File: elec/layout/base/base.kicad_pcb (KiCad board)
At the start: 2 copper layers, 38 parts, among them U1 ?, U2 ?, U3 ?, U4 ?, U5 ?, U6 ?, U7 ?, U8 ?, U9 ?

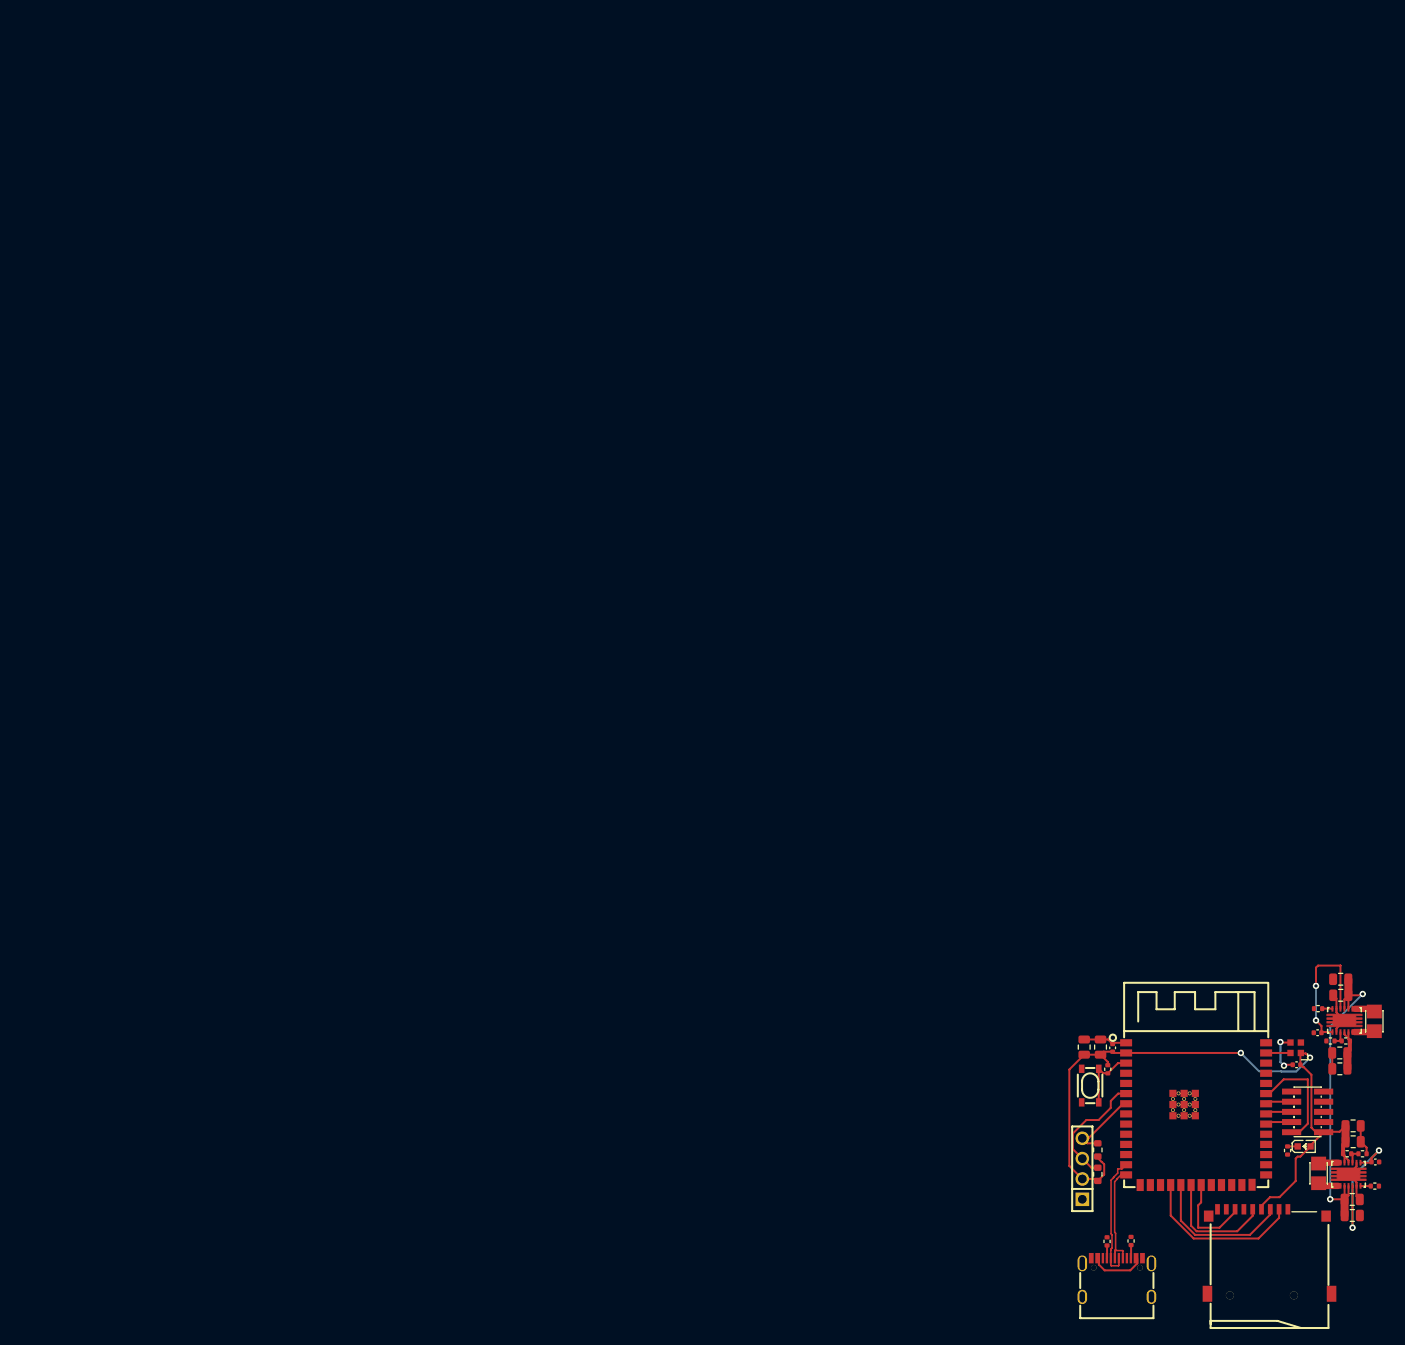
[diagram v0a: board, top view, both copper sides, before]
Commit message: run build with 0.3 compiler
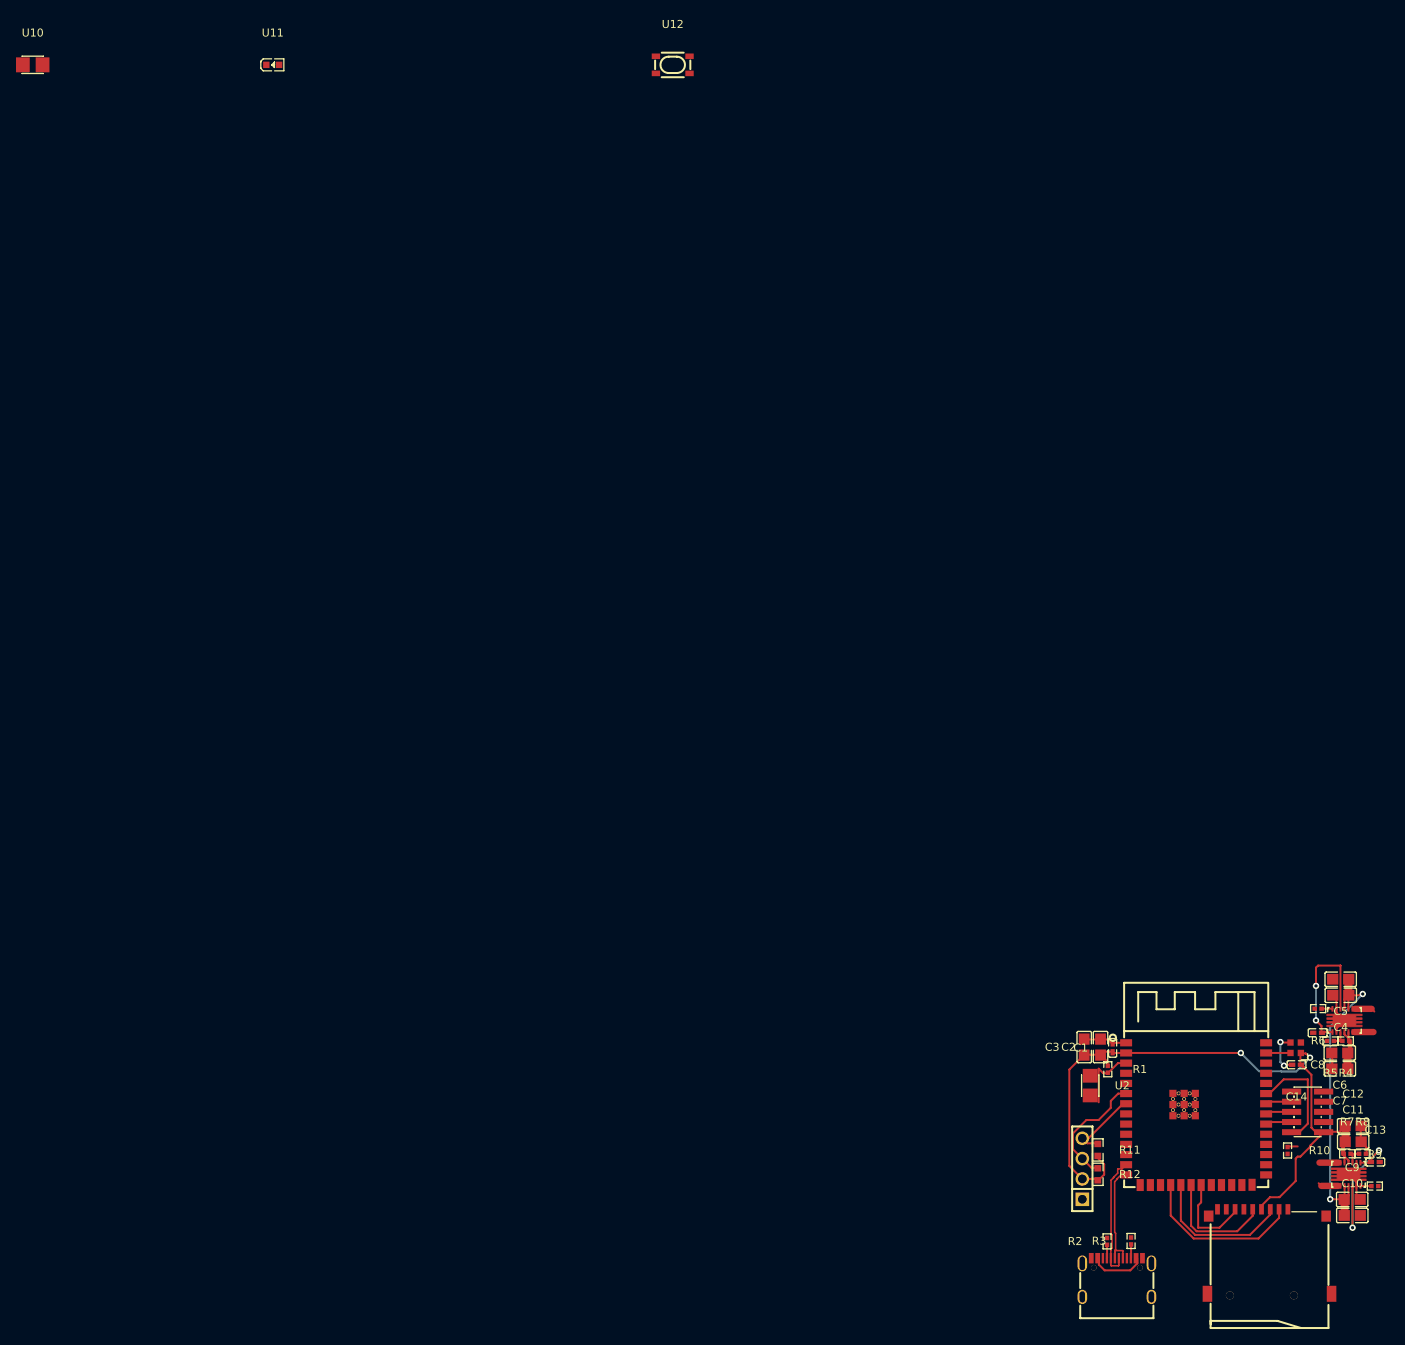
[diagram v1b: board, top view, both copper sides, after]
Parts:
- removed L1, L2: ?, lib:IND-SMD_L2.5-W2.0_WPN252012H
- removed LED1: ?, lib:LED0603-RD
- added U10: , lib:IND-SMD_L2.5-W2.0_WPN252012H, F.Cu at (50.0, 0.00)
- added U11: , lib:LED0603-RD, F.Cu at (80.0, 0.00)
- added U12: , lib:KEY-SMD_4P-L4.2-W3.2-P2.20-LS4.6, F.Cu at (130.0, 0.00)
- C1, C13, C14, C8: value 16V 100nF X7R ±10% 0402 Multilayer Ceramic Capacitors MLCC - SMD/SMT ROHS -> 100nF ±10% 16V X7R; footprint lib:C0402 -> atopile:C0402-b3ef17
- C10, C11, C12, C2, C3, C4, C5, C6, C7, C9: value 25V 10uF X5R ±10% 0805 Multilayer Ceramic Capacitors MLCC - SMD/SMT ROHS -> 10µF ±10% 25V X5R; footprint lib:C0805 -> atopile:C0805-3b2e55
- R1: value 62.5mW Thick Film Resistors 50V ±100ppm/℃ ±1% 10kΩ 0402 Chip Resistor - Surface Mount ROHS -> 10kΩ ±1% 62.5mW; footprint lib:R0402 -> atopile:R0402-56259e
- R10: value 62.5mW Thick Film Resistors 50V ±100ppm/℃ ±1% 330Ω 0402 Chip Resistor - Surface Mount ROHS -> 10kΩ ±1% 62.5mW; footprint lib:R0402 -> atopile:R0402-56259e
- R11, R12: value 100mW Thick Film Resistors 75V ±100ppm/℃ ±1% 2.7kΩ 0603 Chip Resistor - Surface Mount ROHS -> 2.7kΩ ±1% 100mW; footprint lib:R0603 -> atopile:R0603-ebcab9
- R2, R3: value 62.5mW Thick Film Resistors 50V ±100ppm/℃ ±1% 4.7kΩ 0402 Chip Resistor - Surface Mount ROHS -> 4.7kΩ ±1% 62.5mW; footprint lib:R0402 -> atopile:R0402-56259e
- R4: value 62.5mW 50V ±100ppm/℃ ±1% 25.5kΩ 0402 Chip Resistor - Surface Mount ROHS -> 10kΩ ±1% 62.5mW; footprint lib:R0402 -> atopile:R0402-56259e
- R5: value 62.5mW Thick Film Resistors 50V ±1% ±200ppm/℃ 2.8kΩ 0402 Chip Resistor - Surface Mount ROHS -> 10kΩ ±1% 62.5mW; footprint lib:R0402 -> atopile:R0402-56259e
- R6, R9: value 62.5mW Thick Film Resistors 50V ±100ppm/℃ ±1% 1MΩ 0402 Chip Resistor - Surface Mount ROHS -> 1MΩ ±1% 62.5mW; footprint lib:R0402 -> atopile:R0402-56259e
- R7: value 62.5mW Thick Film Resistors 50V ±100ppm/℃ ±1% 23.7kΩ 0402 Chip Resistor - Surface Mount ROHS -> 10kΩ ±1% 62.5mW; footprint lib:R0402 -> atopile:R0402-56259e
- R8: value 62.5mW Thick Film Resistors 50V ±100ppm/℃ ±1% 4.3kΩ 0402 Chip Resistor - Surface Mount ROHS -> 10kΩ ±1% 62.5mW; footprint lib:R0402 -> atopile:R0402-56259e
- U1, U3, U4, U5, U6, U7, U8, U9: value ? -> (none)
- U2: value ? -> (none); footprint lib:KEY-SMD_4P-L4.2-W3.2-P2.20-LS4.6 -> lib:IND-SMD_L2.5-W2.0_WPN252012H
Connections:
- net _3v3_reg.feedback_div-out renamed _3v3_reg-out
- net _3v3_reg.ic-pg renamed _3v3_reg-PG
- net _3v3_reg.ic-vina renamed EN
- net _5v_reg-vcc renamed hv
- net _5v_reg.feedback_div-out renamed _5v_reg-out
- net _5v_reg.ic-l1 renamed _5v_reg-L1
- net _5v_reg.ic-l2 renamed _5v_reg-L2
- net _5v_reg.ic-pg renamed _5v_reg-PG
- net _5v_reg.ic-vina renamed VINA
- net cc1 renamed A5
- net cc2 renamed B5
- net cd renamed CD
- net dat1_rsv_ renamed DAT1_RSV_
- net dat2_rsv_ renamed DAT2_RSV_
- net io1 renamed io
- net rxd0 renamed RXD0
- net sub1 renamed A8
- net sub2 renamed B8
- net txd0 renamed TXD0
- net usb+ renamed dp
- net usb- renamed dm
- net usb_conn-vcc renamed VBUS
- net vcc renamed hv-2
- C1 pad 1: uc.ic-vcc -> hv-1
- C1 pad 2: uc.ic-gnd -> gnd
- C10 pad 2: uc.ic-gnd -> gnd
- C11 pad 1: uc.ic-vcc -> hv-1
- C11 pad 2: uc.ic-gnd -> gnd
- C12 pad 1: uc.ic-vcc -> hv-1
- C12 pad 2: uc.ic-gnd -> gnd
- C13 pad 2: uc.ic-gnd -> gnd
- C14 pad 1: uc.ic-vcc -> hv-1
- C14 pad 2: uc.ic-gnd -> gnd
- C2 pad 1: uc.ic-vcc -> hv-1
- C2 pad 2: uc.ic-gnd -> gnd
- C3 pad 1: uc.ic-vcc -> hv-1
- C3 pad 2: uc.ic-gnd -> gnd
- C4 pad 2: uc.ic-gnd -> gnd
- C5 pad 2: uc.ic-gnd -> gnd
- C6 pad 2: uc.ic-gnd -> gnd
- C7 pad 2: uc.ic-gnd -> gnd
- C8 pad 2: uc.ic-gnd -> gnd
- C9 pad 2: uc.ic-gnd -> gnd
- R1 pad 1: uc.ic-vcc -> hv-1
- R1 pad 2: en -> in
- R10 pad 2: uc.ic-gnd -> gnd
- R11 pad 2: uc.ic-vcc -> hv-1
- R12 pad 2: uc.ic-vcc -> hv-1
- R2 pad 2: uc.ic-gnd -> gnd
- R3 pad 2: uc.ic-gnd -> gnd
- R5 pad 2: uc.ic-gnd -> gnd
- R6 pad 2: uc.ic-gnd -> gnd
- R7 pad 1: uc.ic-vcc -> hv-1
- R8 pad 2: uc.ic-gnd -> gnd
- R9 pad 2: uc.ic-gnd -> gnd
- U1 pad 1: uc.ic-gnd -> gnd
- U1 pad 2: uc.ic-vcc -> hv-1
- U1 pad 3: en -> in
- U1 pad 40: uc.ic-gnd -> gnd
- U1 pad 41: uc.ic-gnd -> gnd
- U2 pad 1: en -> _3v3_reg-L1
- U2 pad 2: en -> _3v3_reg-L2
- U3 pad 1: uc.ic-vcc -> (no net)
- U3 pad 10: reset -> (no net)
- U3 pad 3: uc.ic-gnd -> (no net)
- U3 pad 5: uc.ic-gnd -> (no net)
- U3 pad 7: _7 -> (no net)
- U3 pad 9: uc.ic-gnd -> (no net)
- U4 pad 1: uc.ic-gnd -> gnd
- U4 pad 2: uc.ic-gnd -> gnd
- U4 pad 3: uc.ic-gnd -> gnd
- U4 pad 4: uc.ic-gnd -> gnd
- U4 pad A1: uc.ic-gnd -> gnd
- U4 pad A12: uc.ic-gnd -> gnd
- U4 pad B1: uc.ic-gnd -> gnd
- U4 pad B12: uc.ic-gnd -> gnd
- U5 pad 13: uc.ic-gnd -> gnd
- U5 pad 15: uc.ic-gnd -> gnd
- U5 pad 2: uc.ic-gnd -> gnd
- U6 pad 13: uc.ic-gnd -> gnd
- U6 pad 15: uc.ic-gnd -> gnd
- U6 pad 2: uc.ic-gnd -> gnd
- U6 pad 4: uc.ic-vcc -> hv-1
- U6 pad 5: uc.ic-vcc -> hv-1
- U6 pad 6: _3v3_reg.ic-l2 -> _3v3_reg-L2
- U6 pad 7: _3v3_reg.ic-l2 -> _3v3_reg-L2
- U6 pad 8: _3v3_reg.ic-l1 -> _3v3_reg-L1
- U6 pad 9: _3v3_reg.ic-l1 -> _3v3_reg-L1
- U7 pad 10: uc.ic-gnd -> gnd
- U7 pad 11: uc.ic-gnd -> gnd
- U7 pad 12: uc.ic-gnd -> gnd
- U7 pad 13: uc.ic-gnd -> gnd
- U7 pad 4: uc.ic-vcc -> hv-1
- U7 pad 6: uc.ic-gnd -> gnd
- U8 pad 1: uc.ic-vcc -> hv-1
- U8 pad 3: uc.ic-gnd -> gnd
- U9 pad 1: uc.ic-gnd -> gnd
- U9 pad 2: uc.ic-vcc -> hv-1
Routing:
- net (no net): track 0.00 -> 230.4 mm, vias 0 -> 8
- net uc.ic-vcc: track 91.0 -> 0.00 mm, vias 2 -> 0
- net hv-2: track 42.3 -> 0.00 mm, vias 2 -> 0
- net uc.ic-gnd: track 28.1 -> 0.00 mm, vias 2 -> 0
- net EN: track 19.5 -> 0.00 mm, vias 2 -> 0
- net scl: track 15.3 -> 0.00 mm
- net sda: track 9.46 -> 0.00 mm
- net en: track 8.40 -> 0.00 mm
- net hv-1: track 0.00 -> 6.20 mm
- net hv: track 6.20 -> 0.00 mm
- net _5v_reg-L1: track 2.59 -> 0.00 mm
- net _3v3_reg.ic-l1: track 2.59 -> 0.00 mm
- net _5v_reg-L2: track 2.54 -> 0.00 mm
- net _3v3_reg.ic-l2: track 2.54 -> 0.00 mm
- net out: track 0.00 -> 2.08 mm
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
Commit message: Revert "run build with 0.3 compiler"
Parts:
- removed U10: , lib:IND-SMD_L2.5-W2.0_WPN252012H
- removed U11: , lib:LED0603-RD
- removed U12: , lib:KEY-SMD_4P-L4.2-W3.2-P2.20-LS4.6
- added L1: ?, lib:IND-SMD_L2.5-W2.0_WPN252012H, F.Cu at (217.7, 119.6)
- added L2: ?, lib:IND-SMD_L2.5-W2.0_WPN252012H, F.Cu at (210.7, 138.6)
- added LED1: ?, lib:LED0603-RD, F.Cu at (208.9, 135.2)
- C1, C13, C14, C8: value 100nF ±10% 16V X7R -> 16V 100nF X7R ±10% 0402 Multilayer Ceramic Capacitors MLCC - SMD/SMT ROHS; footprint atopile:C0402-b3ef17 -> lib:C0402
- C10, C11, C12, C2, C3, C4, C5, C6, C7, C9: value 10µF ±10% 25V X5R -> 25V 10uF X5R ±10% 0805 Multilayer Ceramic Capacitors MLCC - SMD/SMT ROHS; footprint atopile:C0805-3b2e55 -> lib:C0805
- R1: value 10kΩ ±1% 62.5mW -> 62.5mW Thick Film Resistors 50V ±100ppm/℃ ±1% 10kΩ 0402 Chip Resistor - Surface Mount ROHS; footprint atopile:R0402-56259e -> lib:R0402
- R10: value 10kΩ ±1% 62.5mW -> 62.5mW Thick Film Resistors 50V ±100ppm/℃ ±1% 330Ω 0402 Chip Resistor - Surface Mount ROHS; footprint atopile:R0402-56259e -> lib:R0402
- R11, R12: value 2.7kΩ ±1% 100mW -> 100mW Thick Film Resistors 75V ±100ppm/℃ ±1% 2.7kΩ 0603 Chip Resistor - Surface Mount ROHS; footprint atopile:R0603-ebcab9 -> lib:R0603
- R2, R3: value 4.7kΩ ±1% 62.5mW -> 62.5mW Thick Film Resistors 50V ±100ppm/℃ ±1% 4.7kΩ 0402 Chip Resistor - Surface Mount ROHS; footprint atopile:R0402-56259e -> lib:R0402
- R4: value 10kΩ ±1% 62.5mW -> 62.5mW 50V ±100ppm/℃ ±1% 25.5kΩ 0402 Chip Resistor - Surface Mount ROHS; footprint atopile:R0402-56259e -> lib:R0402
- R5: value 10kΩ ±1% 62.5mW -> 62.5mW Thick Film Resistors 50V ±1% ±200ppm/℃ 2.8kΩ 0402 Chip Resistor - Surface Mount ROHS; footprint atopile:R0402-56259e -> lib:R0402
- R6, R9: value 1MΩ ±1% 62.5mW -> 62.5mW Thick Film Resistors 50V ±100ppm/℃ ±1% 1MΩ 0402 Chip Resistor - Surface Mount ROHS; footprint atopile:R0402-56259e -> lib:R0402
- R7: value 10kΩ ±1% 62.5mW -> 62.5mW Thick Film Resistors 50V ±100ppm/℃ ±1% 23.7kΩ 0402 Chip Resistor - Surface Mount ROHS; footprint atopile:R0402-56259e -> lib:R0402
- R8: value 10kΩ ±1% 62.5mW -> 62.5mW Thick Film Resistors 50V ±100ppm/℃ ±1% 4.3kΩ 0402 Chip Resistor - Surface Mount ROHS; footprint atopile:R0402-56259e -> lib:R0402
- U1, U3, U4, U5, U6, U7, U8, U9: value (none) -> ?
- U2: value (none) -> ?; footprint lib:IND-SMD_L2.5-W2.0_WPN252012H -> lib:KEY-SMD_4P-L4.2-W3.2-P2.20-LS4.6
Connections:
- net A5 renamed cc1
- net A8 renamed sub1
- net B5 renamed cc2
- net B8 renamed sub2
- net CD renamed cd
- net DAT1_RSV_ renamed dat1_rsv_
- net DAT2_RSV_ renamed dat2_rsv_
- net EN renamed _3v3_reg.ic-vina
- net RXD0 renamed rxd0
- net TXD0 renamed txd0
- net VBUS renamed usb_conn-vcc
- net VINA renamed _5v_reg.ic-vina
- net _3v3_reg-PG renamed _3v3_reg.ic-pg
- net _3v3_reg-out renamed _3v3_reg.feedback_div-out
- net _5v_reg-L1 renamed _5v_reg.ic-l1
- net _5v_reg-L2 renamed _5v_reg.ic-l2
- net _5v_reg-PG renamed _5v_reg.ic-pg
- net _5v_reg-out renamed _5v_reg.feedback_div-out
- net dm renamed usb-
- net dp renamed usb+
- net hv renamed _5v_reg-vcc
- net hv-2 renamed vcc
- net io renamed io1
- C1 pad 1: hv-1 -> uc.ic-vcc
- C1 pad 2: gnd -> uc.ic-gnd
- C10 pad 2: gnd -> uc.ic-gnd
- C11 pad 1: hv-1 -> uc.ic-vcc
- C11 pad 2: gnd -> uc.ic-gnd
- C12 pad 1: hv-1 -> uc.ic-vcc
- C12 pad 2: gnd -> uc.ic-gnd
- C13 pad 2: gnd -> uc.ic-gnd
- C14 pad 1: hv-1 -> uc.ic-vcc
- C14 pad 2: gnd -> uc.ic-gnd
- C2 pad 1: hv-1 -> uc.ic-vcc
- C2 pad 2: gnd -> uc.ic-gnd
- C3 pad 1: hv-1 -> uc.ic-vcc
- C3 pad 2: gnd -> uc.ic-gnd
- C4 pad 2: gnd -> uc.ic-gnd
- C5 pad 2: gnd -> uc.ic-gnd
- C6 pad 2: gnd -> uc.ic-gnd
- C7 pad 2: gnd -> uc.ic-gnd
- C8 pad 2: gnd -> uc.ic-gnd
- C9 pad 2: gnd -> uc.ic-gnd
- R1 pad 1: hv-1 -> uc.ic-vcc
- R1 pad 2: in -> en
- R10 pad 2: gnd -> uc.ic-gnd
- R11 pad 2: hv-1 -> uc.ic-vcc
- R12 pad 2: hv-1 -> uc.ic-vcc
- R2 pad 2: gnd -> uc.ic-gnd
- R3 pad 2: gnd -> uc.ic-gnd
- R5 pad 2: gnd -> uc.ic-gnd
- R6 pad 2: gnd -> uc.ic-gnd
- R7 pad 1: hv-1 -> uc.ic-vcc
- R8 pad 2: gnd -> uc.ic-gnd
- R9 pad 2: gnd -> uc.ic-gnd
- U1 pad 1: gnd -> uc.ic-gnd
- U1 pad 2: hv-1 -> uc.ic-vcc
- U1 pad 3: in -> en
- U1 pad 40: gnd -> uc.ic-gnd
- U1 pad 41: gnd -> uc.ic-gnd
- U2 pad 1: _3v3_reg-L1 -> en
- U2 pad 2: _3v3_reg-L2 -> en
- U3 pad 1: (no net) -> uc.ic-vcc
- U3 pad 10: (no net) -> reset
- U3 pad 3: (no net) -> uc.ic-gnd
- U3 pad 5: (no net) -> uc.ic-gnd
- U3 pad 7: (no net) -> _7
- U3 pad 9: (no net) -> uc.ic-gnd
- U4 pad 1: gnd -> uc.ic-gnd
- U4 pad 2: gnd -> uc.ic-gnd
- U4 pad 3: gnd -> uc.ic-gnd
- U4 pad 4: gnd -> uc.ic-gnd
- U4 pad A1: gnd -> uc.ic-gnd
- U4 pad A12: gnd -> uc.ic-gnd
- U4 pad B1: gnd -> uc.ic-gnd
- U4 pad B12: gnd -> uc.ic-gnd
- U5 pad 13: gnd -> uc.ic-gnd
- U5 pad 15: gnd -> uc.ic-gnd
- U5 pad 2: gnd -> uc.ic-gnd
- U6 pad 13: gnd -> uc.ic-gnd
- U6 pad 15: gnd -> uc.ic-gnd
- U6 pad 2: gnd -> uc.ic-gnd
- U6 pad 4: hv-1 -> uc.ic-vcc
- U6 pad 5: hv-1 -> uc.ic-vcc
- U6 pad 6: _3v3_reg-L2 -> _3v3_reg.ic-l2
- U6 pad 7: _3v3_reg-L2 -> _3v3_reg.ic-l2
- U6 pad 8: _3v3_reg-L1 -> _3v3_reg.ic-l1
- U6 pad 9: _3v3_reg-L1 -> _3v3_reg.ic-l1
- U7 pad 10: gnd -> uc.ic-gnd
- U7 pad 11: gnd -> uc.ic-gnd
- U7 pad 12: gnd -> uc.ic-gnd
- U7 pad 13: gnd -> uc.ic-gnd
- U7 pad 4: hv-1 -> uc.ic-vcc
- U7 pad 6: gnd -> uc.ic-gnd
- U8 pad 1: hv-1 -> uc.ic-vcc
- U8 pad 3: gnd -> uc.ic-gnd
- U9 pad 1: gnd -> uc.ic-gnd
- U9 pad 2: hv-1 -> uc.ic-vcc
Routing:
- net (no net): track 230.4 -> 0.00 mm, vias 8 -> 0
- net uc.ic-vcc: track 0.00 -> 91.0 mm, vias 0 -> 2
- net vcc: track 0.00 -> 42.3 mm, vias 0 -> 2
- net uc.ic-gnd: track 0.00 -> 28.1 mm, vias 0 -> 2
- net _3v3_reg.ic-vina: track 0.00 -> 19.5 mm, vias 0 -> 2
- net scl: track 0.00 -> 15.3 mm
- net sda: track 0.00 -> 9.46 mm
- net en: track 0.00 -> 8.40 mm
- net hv-1: track 6.20 -> 0.00 mm
- net _5v_reg-vcc: track 0.00 -> 6.20 mm
- net _5v_reg.ic-l1: track 0.00 -> 2.59 mm
- net _3v3_reg.ic-l1: track 0.00 -> 2.59 mm
- net _5v_reg.ic-l2: track 0.00 -> 2.54 mm
- net _3v3_reg.ic-l2: track 0.00 -> 2.54 mm
- net out: track 2.08 -> 0.00 mm
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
